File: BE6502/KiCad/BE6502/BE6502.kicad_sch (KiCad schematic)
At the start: 22 parts, among them SW1 SPDT, U1 W65C02SxP, U10 74HC00, U2 W65C22NxP, U3 W65C51NxP, U4 AT28C256, U5 62256, U6 74HC245, U7 74HC244, U8 74HC138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

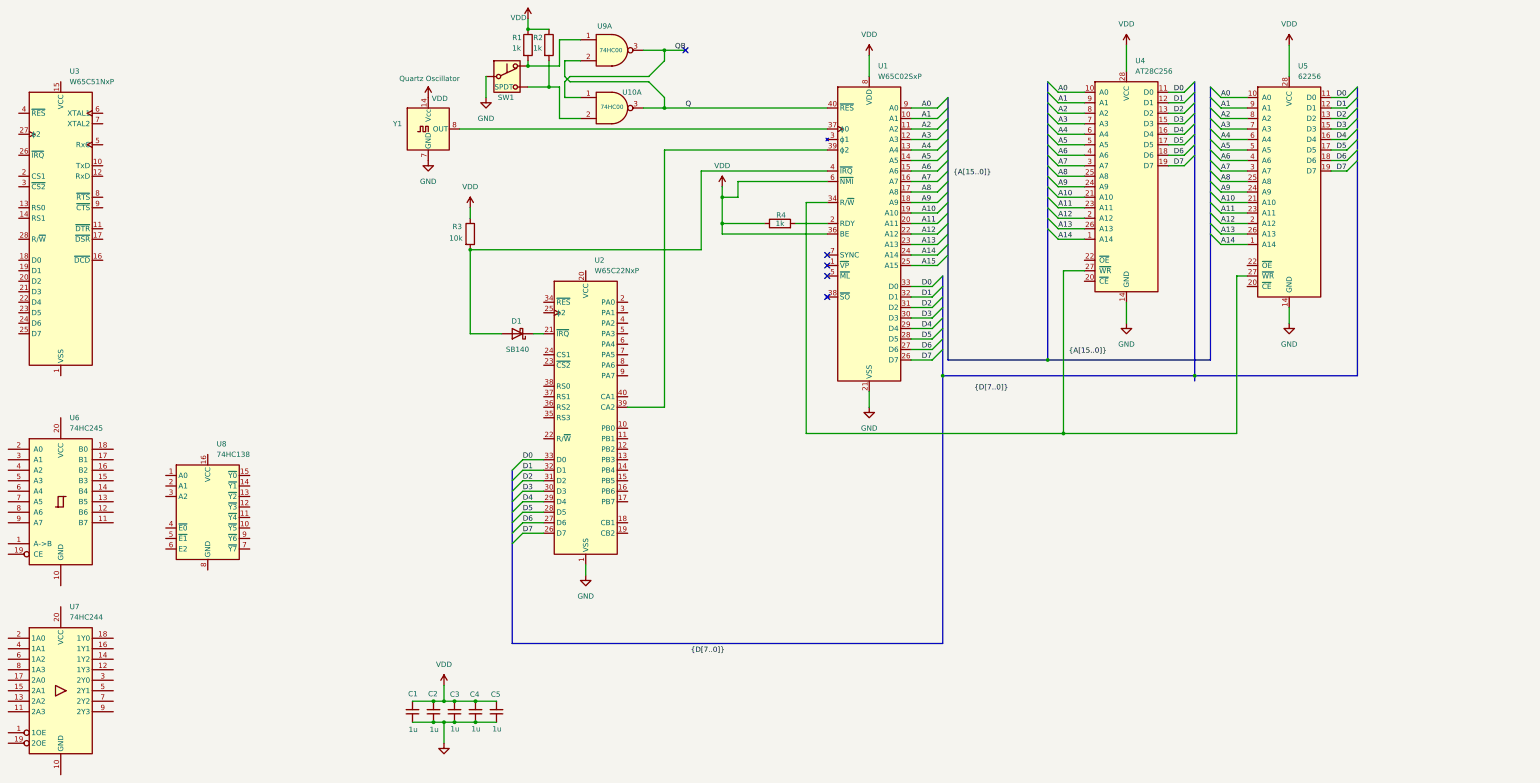
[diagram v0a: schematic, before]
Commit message: kicad updates. start collecting datasheets
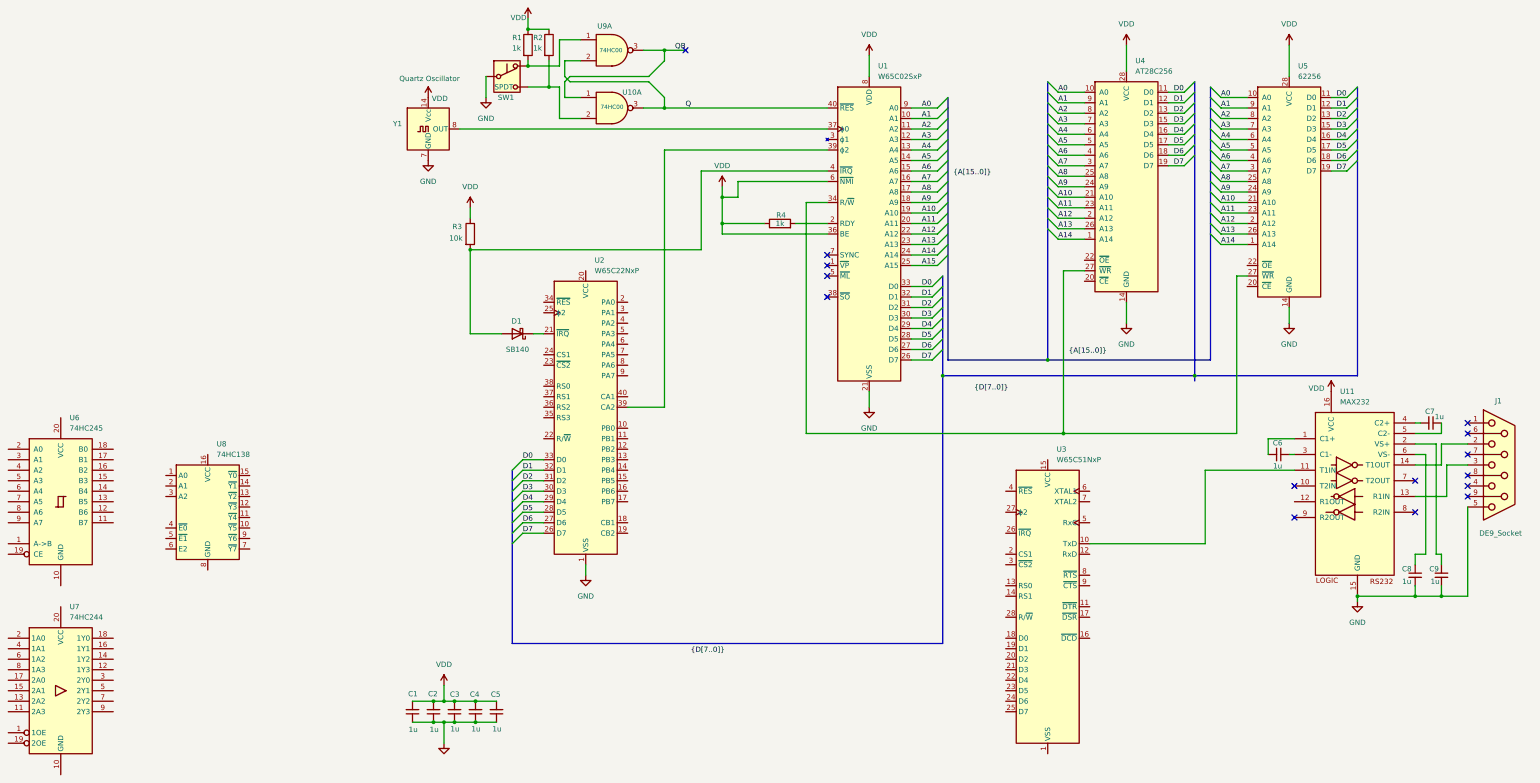
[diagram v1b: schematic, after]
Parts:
- added C6, C7, C8, C9: 1u, symbol Device:C_Small
- added J1: DE9_Socket, symbol Connector:DE9_Socket
- added U11: MAX232, symbol Interface_UART:MAX232
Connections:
- net GND: now also C8.2, C9.2, J1.5, U11.15 (GND)
- net VDD: now also U11.16 (VCC)
- net at U3.10 (TxD): now also U11.11 (T1IN)
- new net: C6.2, U11.1 (C1+)
- new net: J1.3, U11.13 (R1IN)
- new net: J1.2, U11.14 (T1OUT)
- new net: C9.1, U11.2 (VS+)
- new net: C6.1, U11.3 (C1-)
- new net: C7.2, U11.4 (C2+)
- new net: C7.1, U11.5 (C2-)
- new net: C8.1, U11.6 (VS-)
- no-connect marks 5 -> 15
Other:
- moved on the sheet: U3

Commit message: update
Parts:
- removed C1, C2, C3, C4, C5, C6, C7, C8, C9: 1u, symbol Device:C_Small
- removed J1: DE9_Socket, symbol Connector:DE9_Socket
- removed R2, R4: 1k, symbol Device:R
- removed R3: 10k, symbol Device:R
- removed SW1: SPDT, symbol Switch:SW_Push_SPDT
- removed U10, U9: 74HC00, symbol 74xx:74HC00
- removed U11: MAX232, symbol Interface_UART:MAX232
- removed U2: W65C22NxP, Package_DIP:DIP-40_W15.24mm, symbol 6502:W65C22NxP
- removed U3: W65C51NxP, Package_DIP:DIP-28_W15.24mm, symbol 6502:W65C51NxP
- removed U4: AT28C256, symbol 8-bit:AT28C256
- removed U5: 62256, Package_DIP:DIP-28_W15.24mm_Socket, symbol 8-bit:62256
- removed U6: 74HC245, symbol 74xx:74HC245
- removed U7: 74HC244, symbol 74xx:74HC244
- removed U8: 74HC138, symbol 74xx:74HC138
- removed Y1: Quartz Oscillator, Oscillator:Oscillator_DIP-14, symbol Oscillator:ACO-xxxMHz
- added J1: Conn_01x16_Socket, symbol Connector:Conn_01x16_Socket
- added J2: DE9_Pins_MountingHoles, Connector_Dsub:DSUB-9_Pins_Horizontal_P2.77x2.84mm_EdgePinOffset4.94mm_Housed_MountingHolesOffset4.94mm, symbol Connector:DE9_Pins_MountingHoles
- added U2: 28C256, Package_DIP:DIP-28_W15.24mm_Socket, symbol Memory_EEPROM:28C256
- added U3: 74HC00, symbol 74xx:74HC00
- added U4: 62256, Package_DIP:DIP-28_W15.24mm_Socket, symbol 8-bit:62256
- added U5: W65C22NxP, Package_DIP:DIP-40_W15.24mm_Socket, symbol 6502:W65C22NxP
- added U6: MAX232, Package_DIP:DIP-16_W7.62mm_Socket, symbol Interface_UART:MAX232
- added U7: W65C51NxP, Package_DIP:DIP-28_W15.24mm_Socket, symbol 6502:W65C51NxP
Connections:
- net A0: now also U2.10 (A0), U4.10 (A0), U5.38 (RS0)
- net A1: now also U2.9 (A1), U4.9 (A1), U5.37 (RS1)
- net A10: now also U2.21 (A10), U4.21 (A10)
- net A11: now also U2.23 (A11), U4.23 (A11)
- net A12: now also U2.2 (A12), U4.2 (A12)
- net A13: now also U2.26 (A13), U4.26 (A13), U5.24 (CS1)
- net A14: now also U2.1 (A14), U3.4, U4.1 (A14), U4.22 (~{OE})
- net A15: now also U3.12, U3.13
- net A2: now also U2.8 (A2), U4.8 (A2), U5.36 (RS2)
- net A3: now also U2.7 (A3), U4.7 (A3), U5.35 (RS3)
- net A4: now also U2.6 (A4), U4.6 (A4)
- net A5: now also U2.5 (A5), U4.5 (A5)
- net A6: now also U2.4 (A6), U4.4 (A6)
- net A7: now also U2.3 (A7), U4.3 (A7)
- net A8: now also U2.25 (A8), U4.25 (A8)
- net A9: now also U2.24 (A9), U4.24 (A9)
- net D0: now also U2.11 (D0), U4.11 (D0), U5.33 (D0)
- net D1: now also U2.12 (D1), U4.12 (D1), U5.32 (D1)
- net D2: now also U2.13 (D2), U4.13 (D2), U5.31 (D2)
- net D3: now also U2.15 (D3), U4.15 (D3), U5.30 (D3)
- net D4: now also U2.16 (D4), U4.16 (D4), U5.29 (D4)
- net D5: now also U2.17 (D5), U4.17 (D5), U5.28 (D5)
- net D6: now also U2.18 (D6), U4.18 (D6), U5.27 (D6)
- net D7: now also U2.19 (D7), U4.19 (D7), U5.26 (D7)
- net GND: now also U2.14 (GND), U2.22 (~{OE}), U4.14 (GND), U5.1 (VSS)
- net CLOCK: now reaches U1.37 (ϕ0)
- net CLOCK: now also U3.9, U5.25 (ϕ2)
- net at D1.1 (K): now also U5.21 (~{IRQ})
- net IRQB: now reaches D1.2 (A), U1.4 (~{IRQ})
- net R/Wb: now reaches U1.34 (R/~{W})
- net R/Wb: now also U4.27 (~{WR}), U5.22 (R/~{W})
- net at R1.2: now also U1.2 (RDY)
- net Q renamed RESET
- net RESET: now also U5.34 (~{RES})
- net VDD renamed VCC
- net VCC: now also U2.27 (~{WE}), U2.28 (VCC), U4.28 (VCC), U5.20 (VCC)
- new net: U3.8, U4.20 (~{CE})
- new net: U3.6, U5.23 (~{CS2})
- new net: U2.20 (~{CS}), U3.10, U3.11, U3.5
- new net PB0: U5.10 (PB0)
- new net PB1: U5.11 (PB1)
- new net PB2: U5.12 (PB2)
- new net PB3: U5.13 (PB3)
- new net PB4: U5.14 (PB4)
- new net PB5: U5.15 (PB5)
- new net PB6: U5.16 (PB6)
- no-connect marks 15 -> 19
